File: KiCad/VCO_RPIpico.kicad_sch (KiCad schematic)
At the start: 16 parts, among them J1 AudioJack2, J2 Barrel_Jack, SW1 LFO Waveform, SW2 Play

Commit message: Korrektur und KiCad
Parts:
- added RV4, RV5: 100k, Potentiometer_THT:Potentiometer_Alps_RK09K_Single_Vertical, symbol Device:R_Potentiometer
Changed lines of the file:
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@@
+	)
+	(symbol
+		(lib_id "Device:R_Potentiometer")
+		(at 205.74 45.72 90)
+		(mirror x)
+		(unit 1)
+		(exclude_from_sim no)
+		(in_bom yes)
+		(on_board yes)
+		(dnp no)
+		(property "Reference" "RV5"
+			(at 204.47 43.18 90)
+			(effects
+				(font
+					(size 1.27 1.27)
+				)
+				(justify right)
+			)
+		)
+		(property "Value" "100k"
+			(at 203.2 45.72 90)
+			(effects
+				(font
+					(size 1.27 1.27)
+				)
+				(justify right)
+			)
+		)
+		(property "Footprint" "Potentiometer_THT:Potentiometer_Alps_RK09K_Single_Vertical"
+			(at 205.74 45.72 0)
+			(effects
+				(font
+					(size 1.27 1.27)
+				)
+				(hide yes)
+			)
+		)
+		(property "Datasheet" "~"
+			(at 205.74 45.72 0)
+			(effects
+				(font
+					(size 1.27 1.27)
+				)
+				(hide yes)
+			)
+		)
+		(property "Description" ""
+			(at 205.74 45.72 0)
+			(effects
+				(font
+					(size 1.27 1.27)
+				)
+				(hide yes)
+			)
+		)
+		(pin "1"
+		)
+		(pin "2"
+		)
+		(pin "3"
+		)
+		(instances
+			(project "VCO_RPIpico"
+				(path "/0d855e99-162c-4989-8fe3-f98154ec6843"
+					(reference "RV5")
+					(unit 1)
+				)
+			)
+		)
 	)
 	(symbol
@@
 					(unit 1)
 				)
+			)
+		)
+	)
+	(symbol
+		(lib_id "Device:R_Potentiometer")
+		(at 190.5 45.72 90)
+		(mirror x)
+		(unit 1)
+		(exclude_from_sim no)
+		(in_bom yes)
+		(on_board yes)
+		(dnp no)
+		(property "Reference" "RV4"
+			(at 189.23 43.18 90)
+			(effects
+				(font
+					(size 1.27 1.27)
+				)
+				(justify right)
+			)
+		)
+		(property "Value" "100k"
+			(at 187.96 45.72 90)
+			(effects
+				(font
+					(size 1.27 1.27)
+				)
+				(justify right)
+			)
+		)
+		(property "Footprint" "Potentiometer_THT:Potentiometer_Alps_RK09K_Single_Vertical"
+			(at 190.5 45.72 0)
+			(effects
+				(font
+					(size 1.27 1.27)
+				)
+				(hide yes)
+			)
+		)
+		(property "Datasheet" "~"
+			(at 190.5 45.72 0)
+			(effects
+				(font
+					(size 1.27 1.27)
+				)
+				(hide yes)
+			)
+		)
+		(property "Description" ""
+			(at 190.5 45.72 0)
+			(effects
+				(font
+					(size 1.27 1.27)
+				)
+				(hide yes)
+			)
+		)
+		(pin "1"
+		)
+		(pin "2"
+		)
+		(pin "3"
+		)
+		(instances
+			(project "VCO_RPIpico"
+				(path "/0d855e99-162c-4989-8fe3-f98154ec6843"
+					(reference "RV4")
+					(unit 1)
+				)

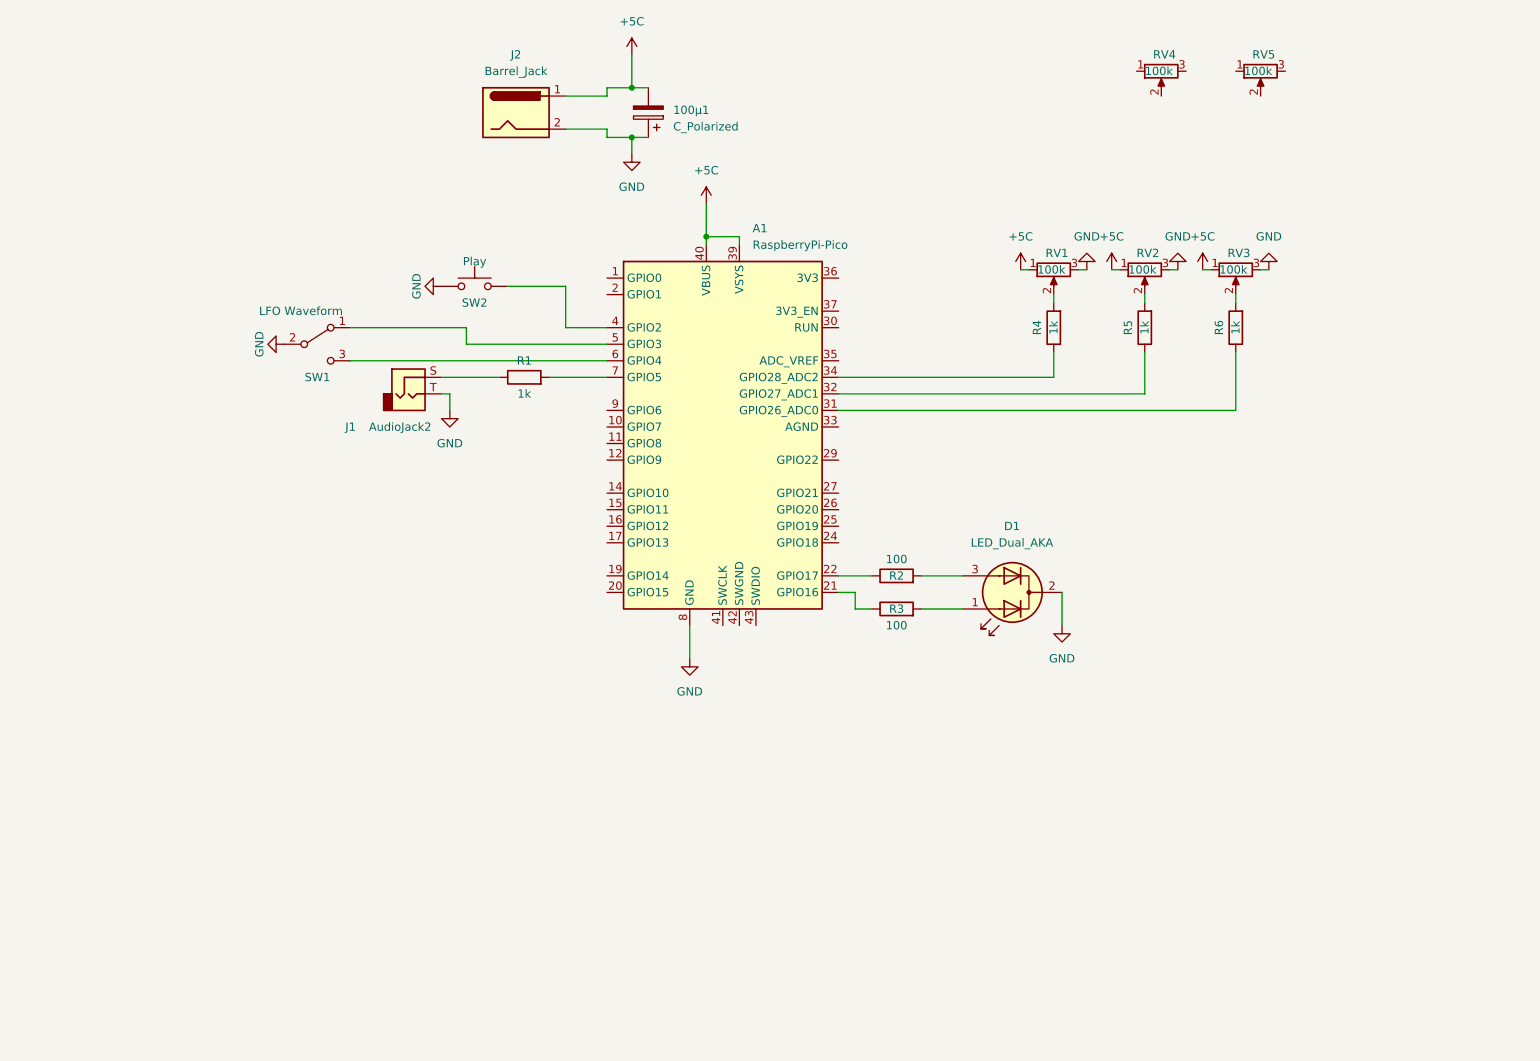
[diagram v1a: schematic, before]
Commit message: Schaltung erweitert um 2 Shhifttasten
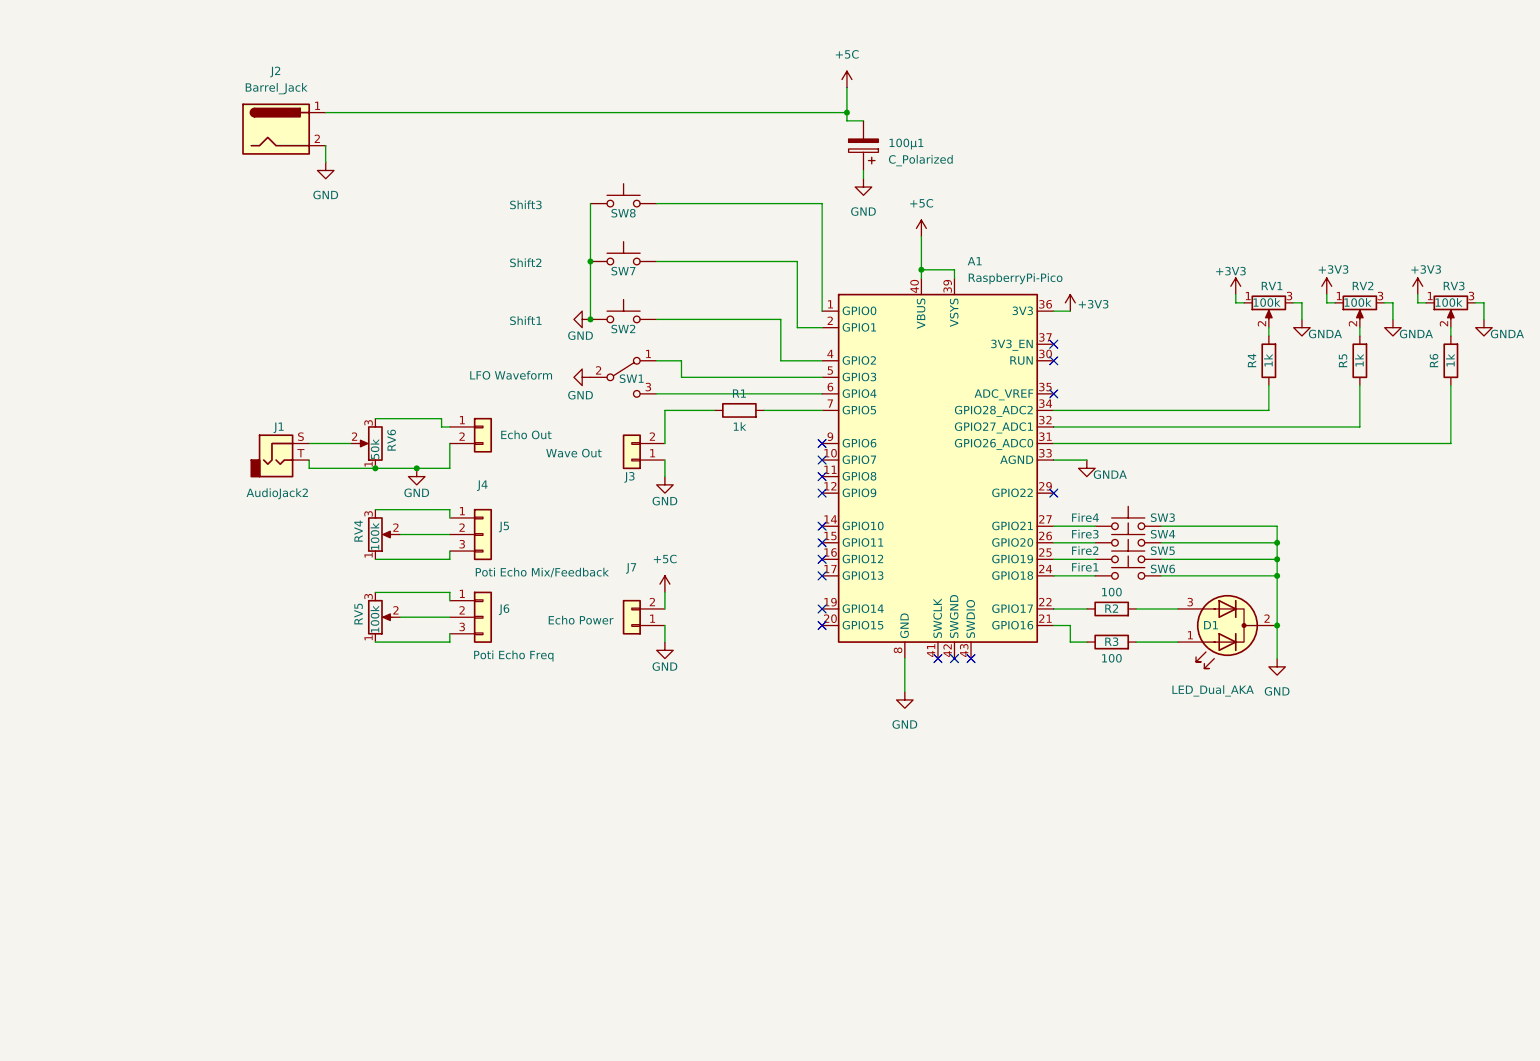
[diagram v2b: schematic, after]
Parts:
- added J3: Wave Out, symbol Connector_Generic:Conn_01x02
- added J4: Echo Out, symbol Connector_Generic:Conn_01x02
- added J5: Poti Echo Mix/Feedback, symbol Connector_Generic:Conn_01x03
- added J6: Poti Echo Freq, symbol Connector_Generic:Conn_01x03
- added J7: Echo Power, symbol Connector_Generic:Conn_01x02
- added RV6: 50k, Potentiometer_THT:Potentiometer_Alps_RK09K_Single_Vertical, symbol Device:R_Potentiometer
- added SW3: Fire4, symbol Switch:SW_Push
- added SW4: Fire3, symbol Switch:SW_Push
- added SW5: Fire2, symbol Switch:SW_Push
- added SW6: Fire1, symbol Switch:SW_Push
- added SW7: Shift2, symbol Switch:SW_Push
- added SW8: Shift3, symbol Switch:SW_Push
- SW2: value Play -> Shift1
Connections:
- net +5C: now also J7.2 (Pin_2); no longer RV1.1, RV2.1, RV3.1
- net GND: now also J3.1 (Pin_1), J4.2 (Pin_2), J7.1 (Pin_1), RV6.1, SW3.2, SW4.2, SW5.2, SW6.2, SW7.1, SW8.1; no longer RV1.3, RV2.3, RV3.3
- net at A1.1 (GPIO0): now also SW8.2
- net at A1.2 (GPIO1): now also SW7.2
- net at A1.24 (GPIO18): now also SW6.1
- net at A1.25 (GPIO19): now also SW5.1
- net at A1.26 (GPIO20): now also SW4.1
- net at A1.27 (GPIO21): now also SW3.1
- net GNDA: now reaches A1.33 (AGND)
- net GNDA: now also RV1.3, RV2.3, RV3.3
- net +3V3: now reaches A1.36 (3V3)
- net +3V3: now also RV1.1, RV2.1, RV3.1
- net at R1.1: now also J3.2 (Pin_2); no longer J1.S
- net at RV5.1: now also J6.3 (Pin_3)
- net at RV5.2: now also J6.2 (Pin_2)
- net at RV5.3: now also J6.1 (Pin_1)
- net at RV4.1: now also J5.3 (Pin_3)
- net at RV4.2: now also J5.2 (Pin_2)
- net at RV4.3: now also J5.1 (Pin_1)
- new net: J1.S, RV6.2
- new net: J4.1 (Pin_1), RV6.3
- no-connect marks 0 -> 17
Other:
- moved on the sheet: 100µ1, A1, D1, J1, J2, R1, R2, R3, R4, R5, R6, RV1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

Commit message: Schaltung geändert
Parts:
- J2: value Barrel_Jack -> Power Jack 5V
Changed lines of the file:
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@@
 			)
 		)
-		(property "Value" "Barrel_Jack"
+		(property "Value" "Power Jack 5V"
 			(at 54.61 48.26 0)
 			(effects

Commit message: Kicad Schematic and Board
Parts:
- removed SW2: Shift1, symbol Switch:SW_Push
- added D2: LED Shift1, LED_THT:LED_D3.0mm, symbol Device:LED
- added D3: LED Shift2, LED_THT:LED_D3.0mm, symbol Device:LED
- added D4: LED Fire1, LED_THT:LED_D3.0mm, symbol Device:LED
- added D5: LED Fire2, LED_THT:LED_D3.0mm, symbol Device:LED
- added D6: LED Fire3, LED_THT:LED_D3.0mm, symbol Device:LED
- added D7: LED Fire4, LED_THT:LED_D3.0mm, symbol Device:LED
- added R10, R11, R12, R7, R8, R9: 100, Resistor_SMD:R_1206_3216Metric, symbol Device:R
- A1: footprint RPI:Raspberry_Pi_Pico_THT -> RPI:Raspberry_Pi_Pico_SMT_THT
- J3, J4, J7: footprint (none) -> Connector_PinSocket_2.54mm:PinSocket_1x02_P2.54mm_Vertical
- J5, J6: footprint (none) -> Connector_PinSocket_2.54mm:PinSocket_1x03_P2.54mm_Vertical
- R1, R2, R3, R4, R5, R6: footprint Resistor_SMD:R_0603_1608Metric -> Resistor_SMD:R_1206_3216Metric
- SW1: footprint (none) -> Button_Switch_THT:SW_Slide-03_Wuerth-WS-SLTV_10x2.5x6.4_P2.54mm
- SW3, SW4, SW5, SW6: footprint (none) -> Button_Switch_THT:SW_PUSH_6mm
- SW7: value Shift2 -> Shift2/Save; footprint (none) -> Button_Switch_THT:SW_PUSH_6mm
- SW8: value Shift3 -> Shift1; footprint (none) -> Button_Switch_THT:SW_PUSH_6mm
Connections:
- net +5C: now also 100µ1.1; no longer 100µ1.2
- net GND: now also 100µ1.2, D2.1 (K), D3.1 (K), D4.1 (K), D5.1 (K), D6.1 (K), D7.1 (K); no longer 100µ1.1
- net at A1.1 (GPIO0): no longer SW8.2
- net at A1.10 (GPIO7): now also SW7.2
- net at A1.11 (GPIO8): now also R7.2
- net at A1.12 (GPIO9): now also R8.2
- net at A1.14 (GPIO10): now also R9.2
- net at A1.15 (GPIO11): now also R10.2
- net at A1.16 (GPIO12): now also R11.2
- net at A1.17 (GPIO13): now also R12.2
- net at A1.2 (GPIO1): no longer SW7.2
- net at A1.9 (GPIO6): now also SW8.2
- new net: D6.2 (A), R11.1
- new net: D4.2 (A), R9.1
- new net: D5.2 (A), R10.1
- new net: D2.2 (A), R7.1
- new net: D7.2 (A), R12.1
- new net: D3.2 (A), R8.1
- no-connect marks 17 -> 12
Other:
- moved on the sheet: 100µ1, J1, J2, J3, J4, J5, J6, J7, RV4, RV5, RV6, SW7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

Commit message: PCB and Schematic
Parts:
- added C2, C3, C4: 100n, Capacitor_SMD:C_1210_3225Metric, symbol Device:C
- A1: footprint RPI:Raspberry_Pi_Pico_SMT_THT -> RPI:Raspberry_Pi_Pico_SMT_THT_noDebugPort
- C1: renamed from 100µ1; value C_Polarized -> 100µ; footprint Capacitor_THT:CP_Radial_D10.0mm_P5.00mm -> Capacitor_SMD:CP_Elec_8x10.5
- D4, D5, D6, D7: footprint LED_THT:LED_D3.0mm -> LED_SMD:LED_1206_3216Metric
- renumbered RV1 to R13, RV2 to R14, RV3 to R15
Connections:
- net GNDA: now also C2.1, C3.1, C4.1
- net at A1.31 (GPIO26_ADC0), R6.1: now also C4.2
- net at A1.32 (GPIO27_ADC1), R5.1: now also C3.2
- net at A1.34 (GPIO28_ADC2), R4.1: now also C2.2
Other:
- note added: "Amount"
- note added: "Freq"
- note added: "Tune"

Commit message: Kicad weiter, Blink
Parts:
- removed D2: LED Shift1, LED_THT:LED_D3.0mm, symbol Device:LED
- removed D3: LED Shift2, LED_THT:LED_D3.0mm, symbol Device:LED
- added D8: LED_Shift2, LED_THT:LED_D3.0mm-3, symbol Device:LED_Dual_AKA
- D1: value LED_Dual_AKA -> LED_Shift1; footprint LED_THT:LED_D5.0mm-3 -> LED_THT:LED_D3.0mm-3
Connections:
- net GND: now also D8.2 (K)
- net at R7.1: now also D8.1 (A1)
- net at R8.1: now also D8.3 (A2)
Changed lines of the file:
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@@
 	)
 	(junction
-		(at 105.41 124.46)
+		(at 105.41 110.49)
 		(diameter 0)
 		(color 0 0 0 0)
 	)
 	(junction
-		(at 213.36 100.33)
+		(at 105.41 124.46)
 		(diameter 0)
 		(color 0 0 0 0)
 	)
 	(junction
-		(at 105.41 113.03)
+		(at 213.36 100.33)
 		(diameter 0)
 		(color 0 0 0 0)
@@
 	)
 	(junction
-		(at 116.84 113.03)
-		(diameter 0)
-		(color 0 0 0 0)
-	)
-	(junction
 		(at 105.41 120.65)
 		(diameter 0)
@@
 	(wire
 		(pts
-			(xy 116.84 107.95) (xy 119.38 107.95)
-		)
-		(stroke
-			(width 0)
-			(type default)
-		)
-	)
-	(wire
-		(pts
 			(xy 45.72 157.48) (xy 46.99 157.48)
 		)
@@
 	(wire
 		(pts
-			(xy 105.41 113.03) (xy 105.41 120.65)
-		)
-		(stroke
-			(width 0)
-			(type default)
-		)
-	)
-	(wire
-		(pts
 			(xy 173.99 100.33) (xy 213.36 100.33)
 		)
@@
 	(wire
 		(pts
-			(xy 119.38 113.03) (xy 116.84 113.03)
-		)
-		(stroke
-			(width 0)
-			(type default)
-		)
-	)
-	(wire
-		(pts
 			(xy 208.28 120.65) (xy 208.28 123.19)
 		)
@@
 	(wire
 		(pts
+			(xy 105.41 110.49) (xy 105.41 120.65)
+		)
+		(stroke
+			(width 0)
+			(type default)
+		)
+	)
+	(wire
+		(pts
 			(xy 226.06 81.28) (xy 226.06 83.82)
 		)
@@
 	(wire
 		(pts
-			(xy 105.41 113.03) (xy 105.41 107.95)
+			(xy 105.41 107.95) (xy 105.41 110.49)
 		)
 		(stroke
@@
 	(wire
 		(pts
+			(xy 105.41 110.49) (xy 111.76 110.49)
+		)
+		(stroke
+			(width 0)
+			(type default)
+		)
+	)
+	(wire
+		(pts
 			(xy 215.9 80.01) (xy 215.9 81.28)
 		)
@@
 	(wire
 		(pts
-			(xy 116.84 113.03) (xy 105.41 113.03)
-		)
-		(stroke
-			(width 0)
-			(type default)
-		)
-	)
-	(wire
-		(pts
 			(xy 173.99 120.65) (xy 180.34 120.65)
 		)
@@
 	(wire
 		(pts
-			(xy 116.84 107.95) (xy 116.84 113.03)
-		)
-		(stroke
-			(width 0)
-			(type default)
-		)
-	)
-	(wire
-		(pts
 			(xy 224.79 81.28) (xy 226.06 81.28)
 		)
@@
 		)
 		(property "Value" "Shift2/Save"
-			(at 98.044 107.696 0)
+			(at 97.79 107.95 0)
 			(effects
 				(font
@@
 	)
 	(symbol
-		(lib_id "Device:LED")
-		(at 123.19 107.95 0)
-		(unit 1)
-		(exclude_from_sim no)
-		(in_bom yes)
-		(on_board yes)
-		(dnp no)
-		(property "Reference" "D2"
-			(at 119.888 106.934 0)
-			(effects
-				(font
-					(size 1.27 1.27)
-				)
-			)
-		)
-		(property "Value" "LED Shift1"
-			(at 122.428 104.394 0)
-			(effects
-				(font
-					(size 1.27 1.27)
-				)
-			)
-		)
-		(property "Footprint" "LED_THT:LED_D3.0mm"
-			(at 123.19 107.95 0)
-			(effects
-				(font
-					(size 1.27 1.27)
-				)
-				(hide yes)
-			)
-		)
-		(property "Datasheet" "~"
-			(at 123.19 107.95 0)
-			(effects
-				(font
-					(size 1.27 1.27)
-				)
-				(hide yes)
-			)
-		)
-		(property "Description" "Light emitting diode"
-			(at 123.19 107.95 0)
-			(effects
-				(font
-					(size 1.27 1.27)
-				)
-				(hide yes)
-			)
-		)
-		(pin "2"
-		)
-		(pin "1"
-		)
-		(instances
-			(project ""
-				(path "/0d855e99-162c-4989-8fe3-f98154ec6843"
-					(reference "D2")
-					(unit 1)
-				)
-			)
-		)
-	)
-	(symbol
 		(lib_id "power:GNDA")
 		(at 196.85 90.17 180)
@@
 			)
 		)
-		(property "Value" "LED_Dual_AKA"
+		(property "Value" "LED_Shift1"
 			(at 198.374 140.716 0)
 			(effects
@@
 			)
 		)
-		(property "Footprint" "LED_THT:LED_D5.0mm-3"
+		(property "Footprint" "LED_THT:LED_D3.0mm-3"
 			(at 200.66 130.81 0)
 			(effects
@@
 	)
 	(symbol
-		(lib_id "Device:LED")
-		(at 123.19 113.03 0)
-		(unit 1)
-		(exclude_from_sim no)
-		(in_bom yes)
-		(on_board yes)
-		(dnp no)
-		(property "Reference" "D3"
-			(at 119.888 112.014 0)
-			(effects
-				(font
-					(size 1.27 1.27)
-				)
-			)
-		)
-		(property "Value" "LED Shift2"
-			(at 123.19 116.586 0)
-			(effects
-				(font
-					(size 1.27 1.27)
-				)
-			)
-		)
-		(property "Footprint" "LED_THT:LED_D3.0mm"
-			(at 123.19 113.03 0)
-			(effects
-				(font
-					(size 1.27 1.27)
-				)
-				(hide yes)
-			)
-		)
-		(property "Datasheet" "~"
-			(at 123.19 113.03 0)
-			(effects
-				(font
-					(size 1.27 1.27)
-				)
-				(hide yes)
-			)
-		)
-		(property "Description" "Light emitting diode"
-			(at 123.19 113.03 0)
-			(effects
-				(font
-					(size 1.27 1.27)
-				)
-				(hide yes)
-			)
-		)
-		(pin "2"
-		)
-		(pin "1"
-		)
-		(instances
-			(project "VCO_RPIpico"
-				(path "/0d855e99-162c-4989-8fe3-f98154ec6843"
-					(reference "D3")
-					(unit 1)
-				)
-			)
-		)
-	)
-	(symbol
 		(lib_id "Device:R")
 		(at 207.01 90.17 180)
@@
 					(unit 1)
 				)
+			)
+		)
+	)
+	(symbol
+		(lib_id "Device:LED_Dual_AKA")
+		(at 119.38 110.49 0)
+		(unit 1)
+		(exclude_from_sim no)
+		(in_bom yes)
+		(on_board yes)
+		(dnp no)
+		(property "Reference" "D8"
+			(at 121.92 110.49 0)
+			(effects
+				(font
+					(size 1.27 1.27)
+				)
+			)
+		)
+		(property "Value" "LED_Shift2"
+			(at 118.11 116.84 0)
+			(effects
+				(font
+					(size 1.27 1.27)
+				)
+			)
+		)
+		(property "Footprint" "LED_THT:LED_D3.0mm-3"
+			(at 119.38 110.49 0)
+			(effects
+				(font
+					(size 1.27 1.27)
+				)
+				(hide yes)
+			)
+		)
+		(property "Datasheet" "~"
+			(at 119.38 110.49 0)
+			(effects
+				(font
+					(size 1.27 1.27)
+				)
+				(hide yes)
+			)
+		)
+		(property "Description" ""
+			(at 119.38 110.49 0)
+			(effects
+				(font
+					(size 1.27 1.27)
+				)
+				(hide yes)
+			)
+		)
+		(pin "1"
+		)
+		(pin "2"
+		)
+		(pin "3"
+		)
+		(instances
+			(project "VCO_RPIpico"
+				(path "/0d855e99-162c-4989-8fe3-f98154ec6843"
+					(reference "D8")
+					(unit 1)
+				)

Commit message: Kicad
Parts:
- D4, D5, D6, D7: footprint LED_SMD:LED_1206_3216Metric -> LED_THT:LED_D3.0mm
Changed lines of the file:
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@@
 			)
 		)
-		(property "Footprint" "LED_SMD:LED_1206_3216Metric"
+		(property "Footprint" "LED_THT:LED_D3.0mm"
 			(at 109.22 124.46 0)
 			(effects
@@
 			)
 		)
-		(property "Footprint" "LED_SMD:LED_1206_3216Metric"
+		(property "Footprint" "LED_THT:LED_D3.0mm"
 			(at 109.22 120.65 0)
 			(effects
@@
 			)
 		)
-		(property "Footprint" "LED_SMD:LED_1206_3216Metric"
+		(property "Footprint" "LED_THT:LED_D3.0mm"
 			(at 109.22 132.08 0)
 			(effects
@@
 			)
 		)
-		(property "Footprint" "LED_SMD:LED_1206_3216Metric"
+		(property "Footprint" "LED_THT:LED_D3.0mm"
 			(at 109.22 128.27 0)
 			(effects
